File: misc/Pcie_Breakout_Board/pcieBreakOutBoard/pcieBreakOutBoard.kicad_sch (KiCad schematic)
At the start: 4 parts, among them J1 2041119-1 (Mini Pcie Express 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, J2 Conn_01x14, J3 Conn_01x14, J4 Conn_02x12_Odd_Even

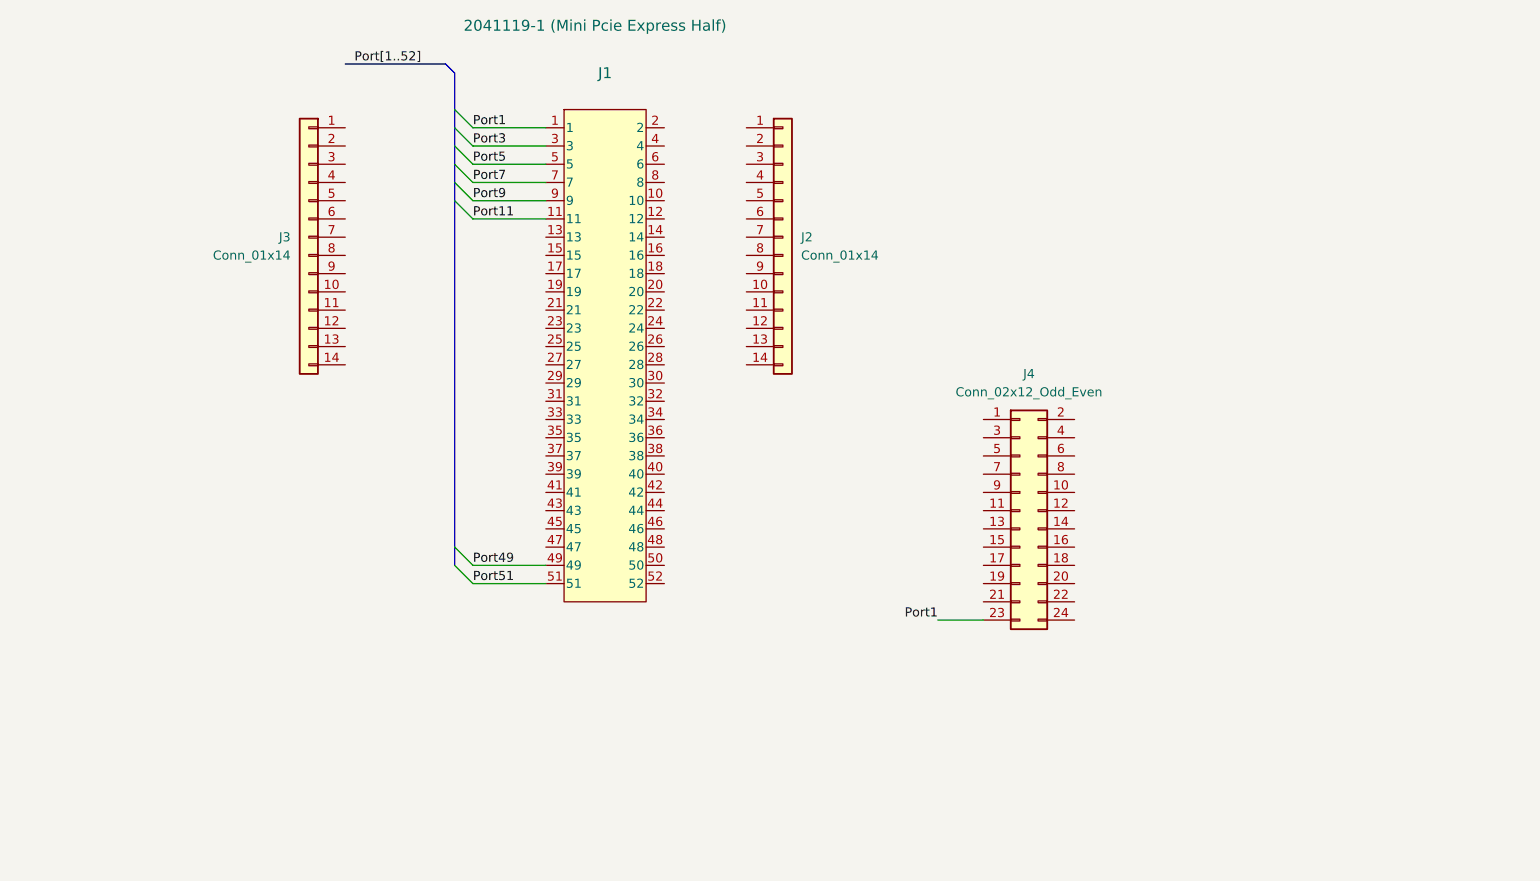
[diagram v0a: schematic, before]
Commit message: PCI Express
Create breakout board for the PCI express mini card half
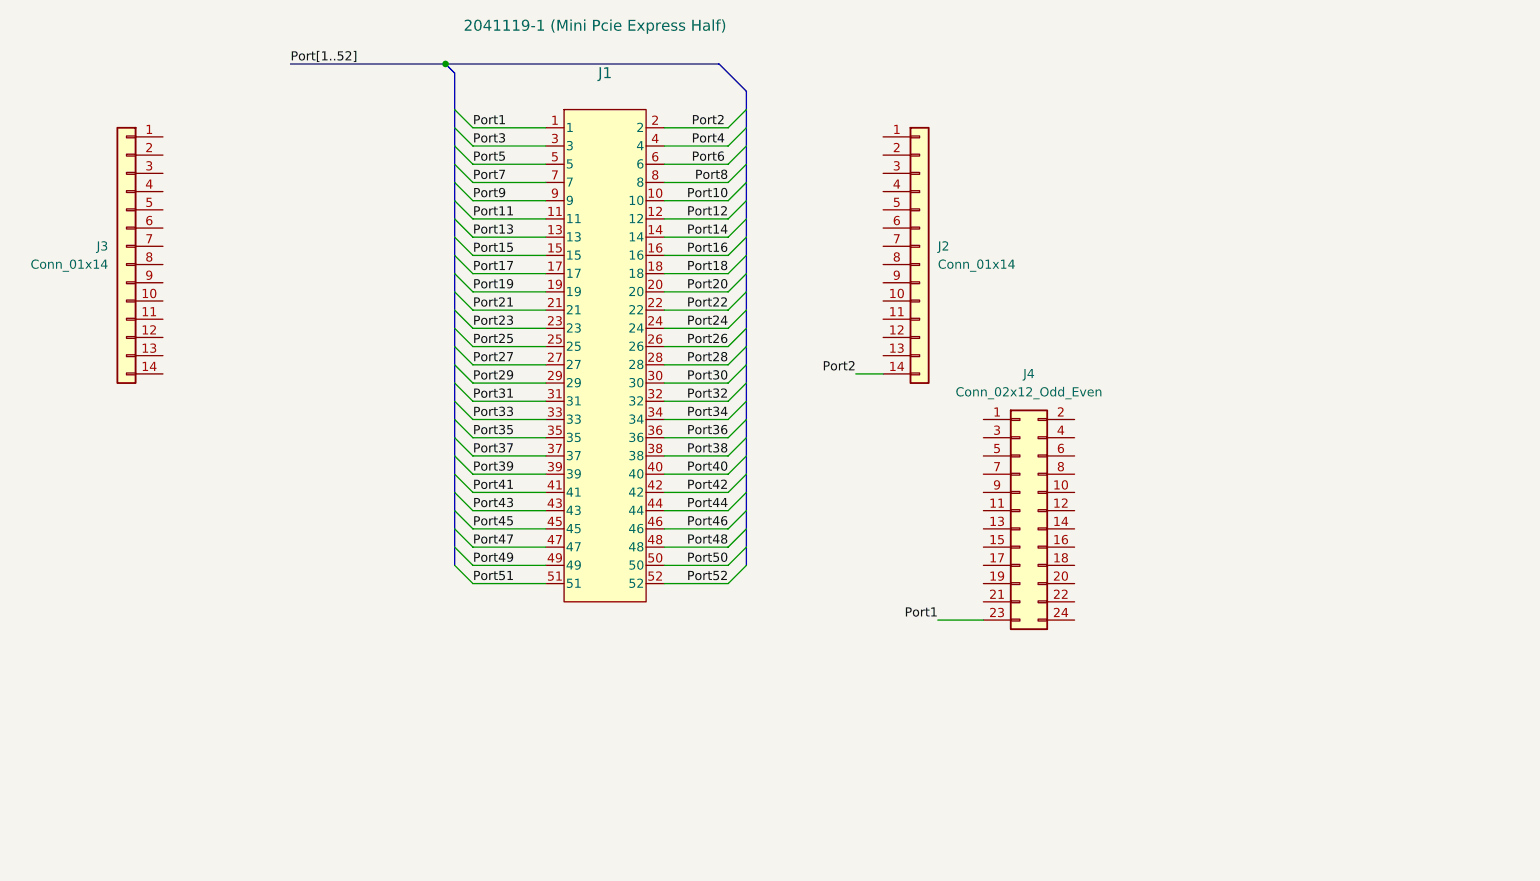
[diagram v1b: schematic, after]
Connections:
- net Port10: now reaches J1.10
- net Port12: now reaches J1.12
- net Port13: now reaches J1.13
- net Port14: now reaches J1.14
- net Port15: now reaches J1.15
- net Port16: now reaches J1.16
- net Port17: now reaches J1.17
- net Port18: now reaches J1.18
- net Port19: now reaches J1.19
- net Port2: now reaches J1.2
- net Port2: now also J2.14 (Pin_14)
- net Port20: now reaches J1.20
- net Port21: now reaches J1.21
- net Port22: now reaches J1.22
- net Port23: now reaches J1.23
- net Port24: now reaches J1.24
- net Port25: now reaches J1.25
- net Port26: now reaches J1.26
- net Port27: now reaches J1.27
- net Port28: now reaches J1.28
- net Port29: now reaches J1.29
- net Port30: now reaches J1.30
- net Port31: now reaches J1.31
- net Port32: now reaches J1.32
- net Port33: now reaches J1.33
- net Port34: now reaches J1.34
- net Port35: now reaches J1.35
- net Port36: now reaches J1.36
- net Port37: now reaches J1.37
- net Port38: now reaches J1.38
- net Port39: now reaches J1.39
- net Port4: now reaches J1.4
- net Port40: now reaches J1.40
- net Port41: now reaches J1.41
- net Port42: now reaches J1.42
- net Port43: now reaches J1.43
- net Port44: now reaches J1.44
- net Port45: now reaches J1.45
- net Port46: now reaches J1.46
- net Port47: now reaches J1.47
- net Port48: now reaches J1.48
- net Port50: now reaches J1.50
- net Port52: now reaches J1.52
- net Port6: now reaches J1.6
- net Port8: now reaches J1.8
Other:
- moved on the sheet: J3

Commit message: pci express Breakoutt Board
Finished routing
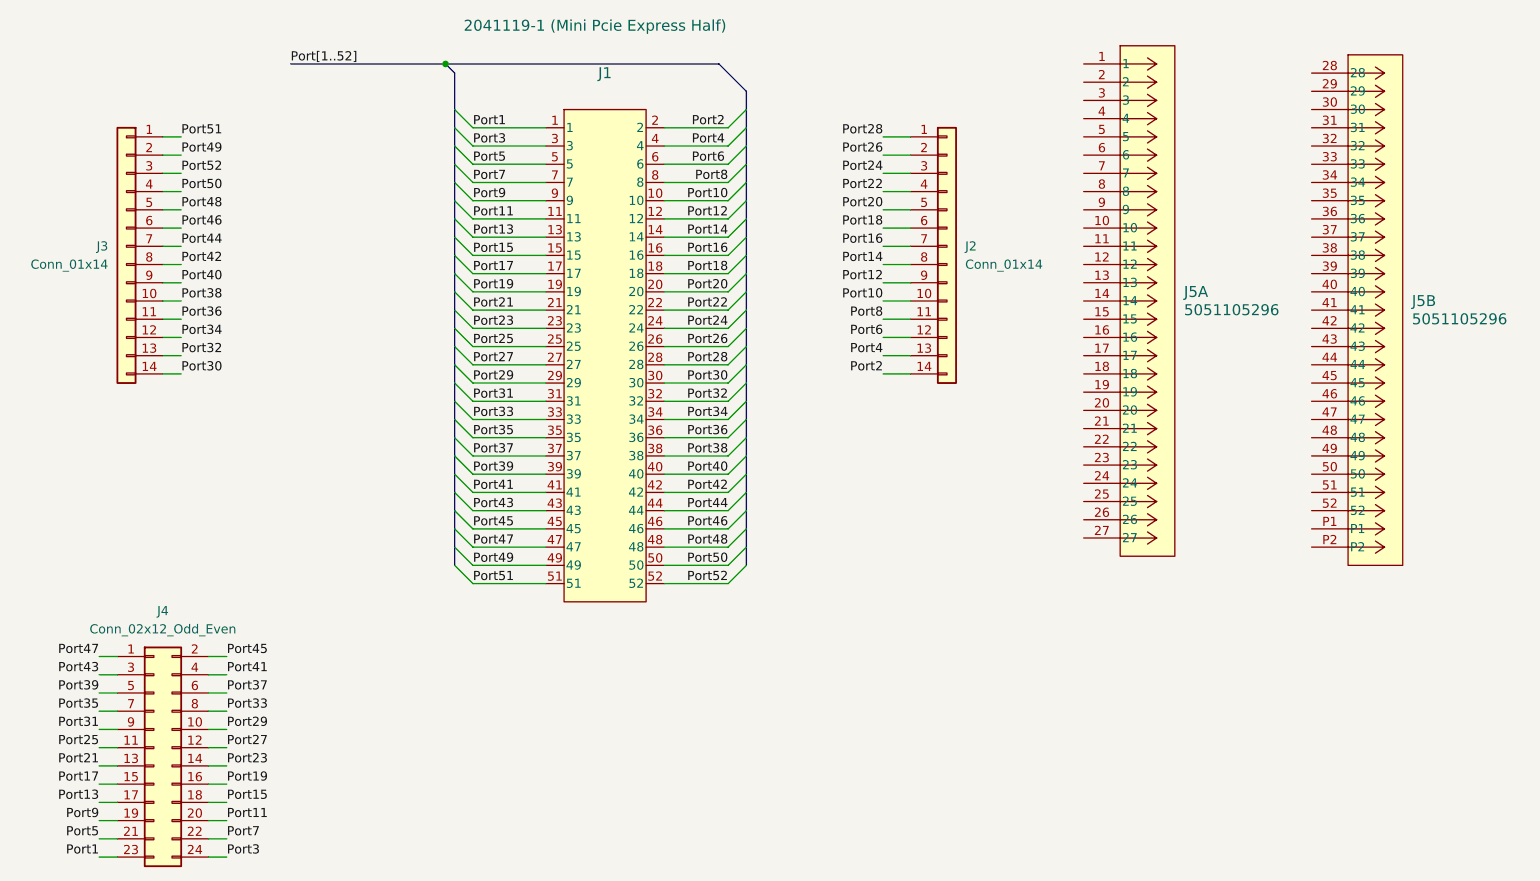
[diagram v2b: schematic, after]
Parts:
- added J5: 5051105296, User_Footprint:CON_5051105296_MOL, symbol _Connectors:5051105296
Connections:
- net Port10: now also J2.10 (Pin_10)
- net Port11: now also J4.20 (Pin_20)
- net Port12: now also J2.9 (Pin_9)
- net Port13: now also J4.17 (Pin_17)
- net Port14: now also J2.8 (Pin_8)
- net Port15: now also J4.18 (Pin_18)
- net Port16: now also J2.7 (Pin_7)
- net Port17: now also J4.15 (Pin_15)
- net Port18: now also J2.6 (Pin_6)
- net Port19: now also J4.16 (Pin_16)
- net Port20: now also J2.5 (Pin_5)
- net Port21: now also J4.13 (Pin_13)
- net Port22: now also J2.4 (Pin_4)
- net Port23: now also J4.14 (Pin_14)
- net Port24: now also J2.3 (Pin_3)
- net Port25: now also J4.11 (Pin_11)
- net Port26: now also J2.2 (Pin_2)
- net Port27: now also J4.12 (Pin_12)
- net Port28: now also J2.1 (Pin_1)
- net Port29: now also J4.10 (Pin_10)
- net Port3: now also J4.24 (Pin_24)
- net Port30: now also J3.14 (Pin_14)
- net Port31: now also J4.9 (Pin_9)
- net Port32: now also J3.13 (Pin_13)
- net Port33: now also J4.8 (Pin_8)
- net Port34: now also J3.12 (Pin_12)
- net Port35: now also J4.7 (Pin_7)
- net Port36: now also J3.11 (Pin_11)
- net Port37: now also J4.6 (Pin_6)
- net Port38: now also J3.10 (Pin_10)
- net Port39: now also J4.5 (Pin_5)
- net Port4: now also J2.13 (Pin_13)
- net Port40: now also J3.9 (Pin_9)
- net Port41: now also J4.4 (Pin_4)
- net Port42: now also J3.8 (Pin_8)
- net Port43: now also J4.3 (Pin_3)
- net Port44: now also J3.7 (Pin_7)
- net Port45: now also J4.2 (Pin_2)
- net Port46: now also J3.6 (Pin_6)
- net Port47: now also J4.1 (Pin_1)
- net Port48: now also J3.5 (Pin_5)
- net Port49: now also J3.2 (Pin_2)
- net Port5: now also J4.21 (Pin_21)
- net Port50: now also J3.4 (Pin_4)
- net Port51: now also J3.1 (Pin_1)
- net Port52: now also J3.3 (Pin_3)
- net Port6: now also J2.12 (Pin_12)
- net Port7: now also J4.22 (Pin_22)
- net Port8: now also J2.11 (Pin_11)
- net Port9: now also J4.19 (Pin_19)
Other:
- moved on the sheet: J2, J4

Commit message: dirctories
Add and remove directories
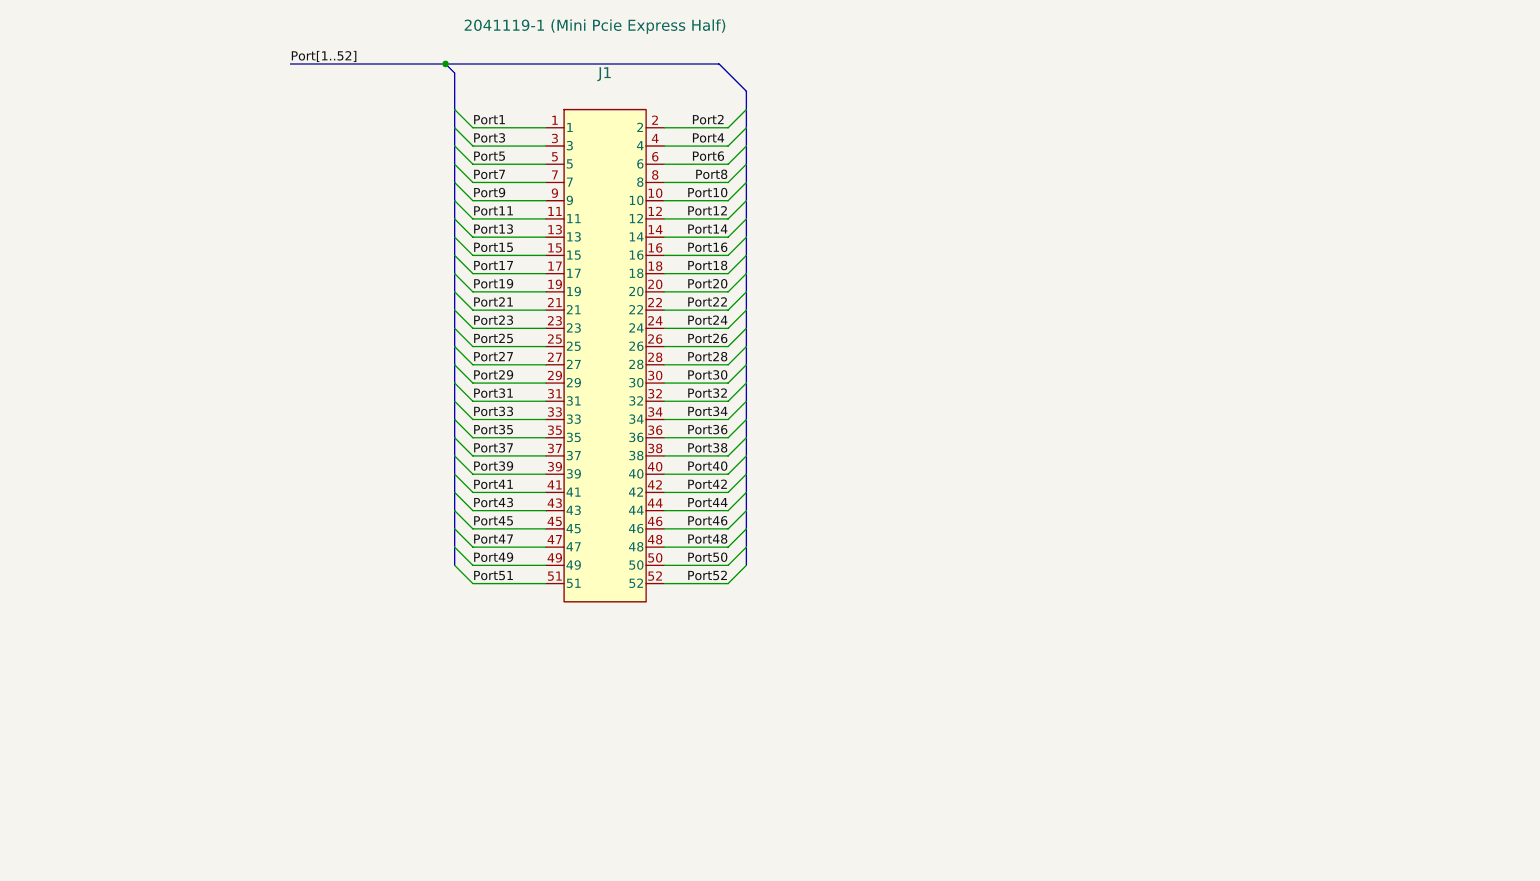
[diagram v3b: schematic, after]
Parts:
- removed J2, J3: Conn_01x14, Connector_PinHeader_2.54mm:PinHeader_1x14_P2.54mm_Vertical_SMD_Pin1Left, symbol Connector_Generic:Conn_01x14
- removed J4: Conn_02x12_Odd_Even, Connector_PinHeader_2.54mm:PinHeader_2x12_P2.54mm_Horizontal, symbol Connector_Generic:Conn_02x12_Odd_Even
- removed J5: 5051105296, User_Footprint:CON_5051105296_MOL, symbol _Connectors:5051105296
